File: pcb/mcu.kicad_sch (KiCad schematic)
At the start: 24 parts

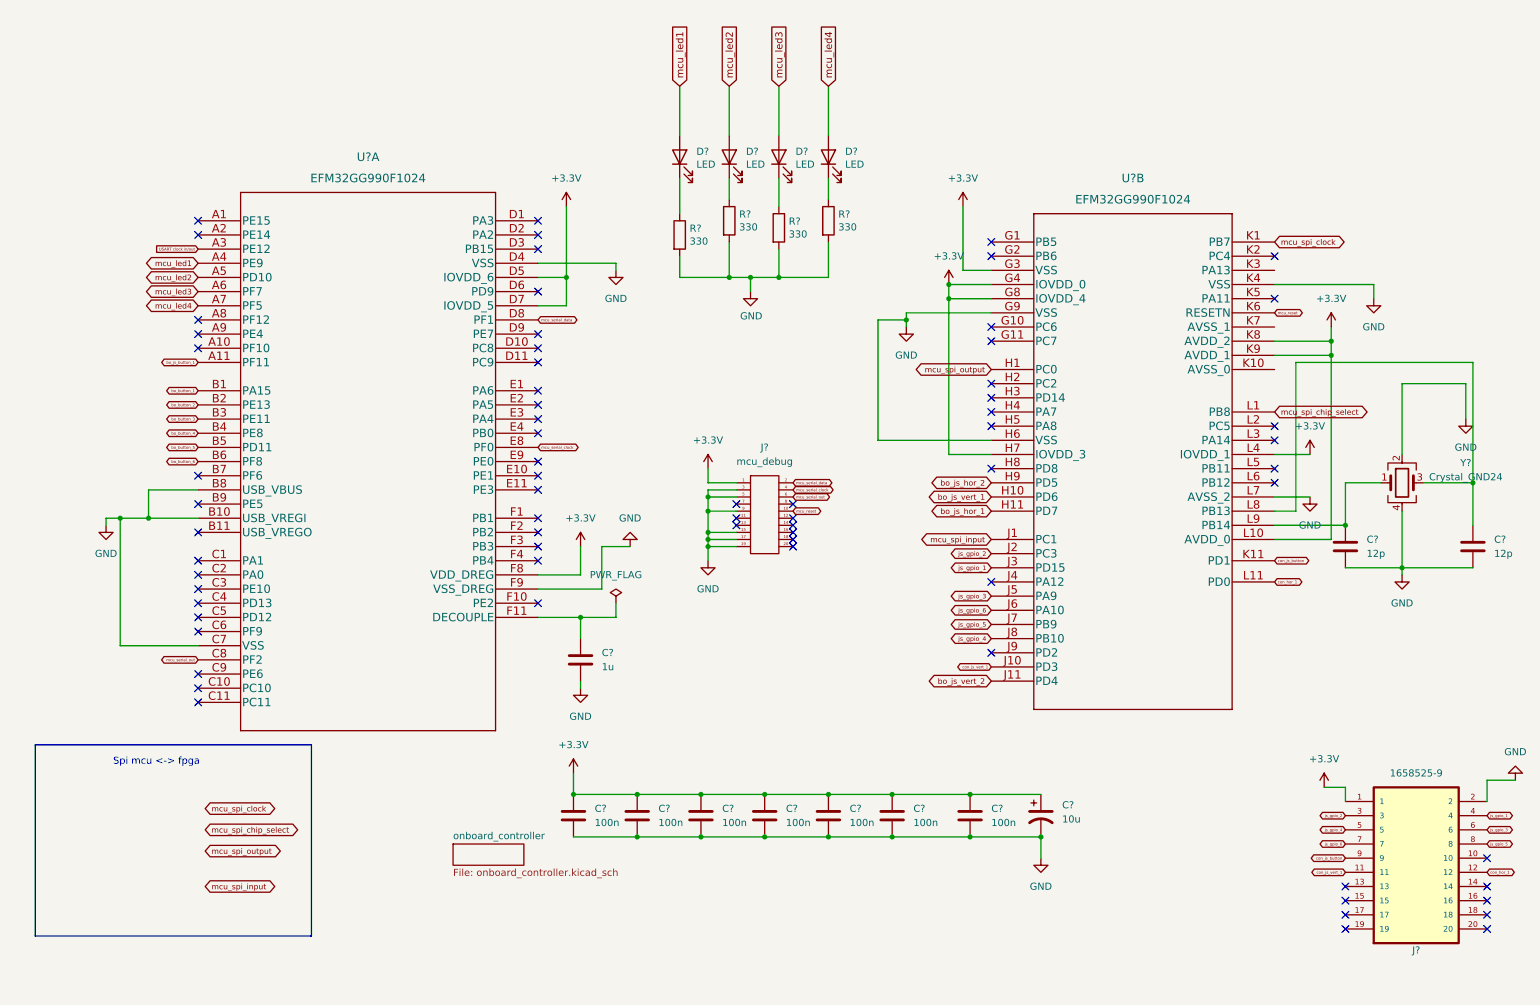
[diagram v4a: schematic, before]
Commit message: add capasitor values
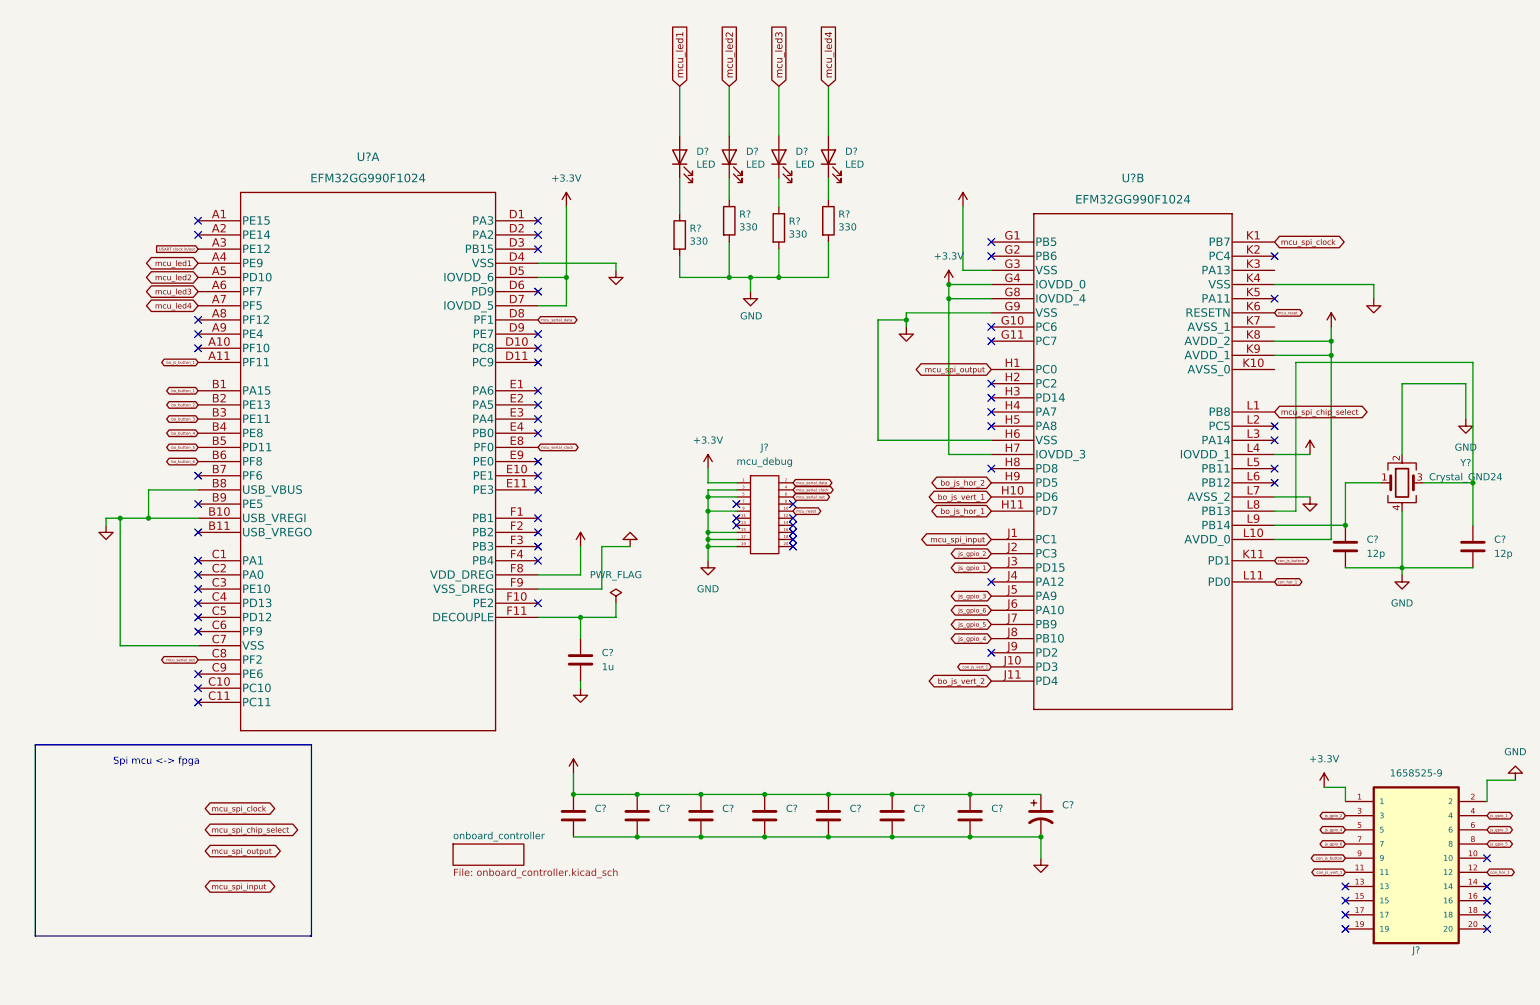
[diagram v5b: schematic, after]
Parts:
- C? (x7): value 100n -> (none)
- C?: value 10u -> (none)
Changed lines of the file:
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@@
       (effects (font (size 1.27 1.27)) hide)
     )
-    (property "Value" "+3.3V" (id 1) (at 111.76 142.24 0))
+    (property "Value" "" (id 1) (at 111.76 142.24 0))
     (property "Footprint" "" (id 2) (at 111.76 147.32 0)
       (effects (font (size 1.27 1.27)) hide)
@@
       (effects (font (size 1.27 1.27)) (justify left))
     )
-    (property "Value" "100n" (id 1) (at 172.72 156.2099 0)
+    (property "Value" "" (id 1) (at 172.72 156.2099 0)
       (effects (font (size 1.27 1.27)) (justify left))
     )
@@
       (effects (font (size 1.27 1.27)) hide)
     )
-    (property "Value" "GND" (id 1) (at 171.45 72.39 0))
+    (property "Value" "" (id 1) (at 171.45 72.39 0))
     (property "Footprint" "" (id 2) (at 171.45 67.31 0)
       (effects (font (size 1.27 1.27)) hide)
@@
       (effects (font (size 1.27 1.27)) hide)
     )
-    (property "Value" "+3.3V" (id 1) (at 243.84 85.09 0))
+    (property "Value" "" (id 1) (at 243.84 85.09 0))
     (property "Footprint" "" (id 2) (at 243.84 90.17 0)
       (effects (font (size 1.27 1.27)) hide)
@@
       (effects (font (size 1.27 1.27)) hide)
     )
-    (property "Value" "GND" (id 1) (at 27.94 107.95 0))
+    (property "Value" "" (id 1) (at 27.94 107.95 0))
     (property "Footprint" "" (id 2) (at 27.94 102.87 0)
       (effects (font (size 1.27 1.27)) hide)
@@
       (effects (font (size 1.27 1.27)) hide)
     )
-    (property "Value" "GND" (id 1) (at 243.84 102.87 0))
+    (property "Value" "" (id 1) (at 243.84 102.87 0))
     (property "Footprint" "" (id 2) (at 243.84 97.79 0)
       (effects (font (size 1.27 1.27)) hide)
@@
       (effects (font (size 1.27 1.27)) (justify left))
     )
-    (property "Value" "100n" (id 1) (at 161.29 156.2099 0)
+    (property "Value" "" (id 1) (at 161.29 156.2099 0)
       (effects (font (size 1.27 1.27)) (justify left))
     )
@@
       (effects (font (size 1.27 1.27)) hide)
     )
-    (property "Value" "GND" (id 1) (at 195.58 167.64 0))
+    (property "Value" "" (id 1) (at 195.58 167.64 0))
     (property "Footprint" "" (id 2) (at 195.58 162.56 0)
       (effects (font (size 1.27 1.27)) hide)
@@
       (effects (font (size 1.27 1.27)) hide)
     )
-    (property "Value" "GND" (id 1) (at 121.92 101.6 0))
+    (property "Value" "" (id 1) (at 121.92 101.6 0))
     (property "Footprint" "" (id 2) (at 121.92 106.68 0)
       (effects (font (size 1.27 1.27)) hide)
@@
       (effects (font (size 1.27 1.27)) hide)
     )
-    (property "Value" "GND" (id 1) (at 113.03 137.16 0))
+    (property "Value" "" (id 1) (at 113.03 137.16 0))
     (property "Footprint" "" (id 2) (at 113.03 132.08 0)
       (effects (font (size 1.27 1.27)) hide)
@@
       (effects (font (size 1.27 1.27)) hide)
     )
-    (property "Value" "+3.3V" (id 1) (at 247.65 62.23 0))
+    (property "Value" "" (id 1) (at 247.65 62.23 0))
     (property "Footprint" "" (id 2) (at 247.65 67.31 0)
       (effects (font (size 1.27 1.27)) hide)
@@
       (effects (font (size 1.27 1.27)) hide)
     )
-    (property "Value" "GND" (id 1) (at 255.27 67.31 0))
+    (property "Value" "" (id 1) (at 255.27 67.31 0))
     (property "Footprint" "" (id 2) (at 255.27 62.23 0)
       (effects (font (size 1.27 1.27)) hide)
@@
       (effects (font (size 1.27 1.27)) hide)
     )
-    (property "Value" "+3.3V" (id 1) (at 181.61 40.64 0))
+    (property "Value" "" (id 1) (at 181.61 40.64 0))
     (property "Footprint" "" (id 2) (at 181.61 45.72 0)
       (effects (font (size 1.27 1.27)) hide)
@@
       (effects (font (size 1.27 1.27)) hide)
     )
-    (property "Value" "GND" (id 1) (at 119.38 62.23 0))
+    (property "Value" "" (id 1) (at 119.38 62.23 0))
     (property "Footprint" "" (id 2) (at 119.38 57.15 0)
       (effects (font (size 1.27 1.27)) hide)
@@
       (effects (font (size 1.27 1.27)) hide)
     )
-    (property "Value" "+3.3V" (id 1) (at 113.03 101.6 0))
+    (property "Value" "" (id 1) (at 113.03 101.6 0))
     (property "Footprint" "" (id 2) (at 113.03 106.68 0)
       (effects (font (size 1.27 1.27)) hide)
@@
       (effects (font (size 1.27 1.27)) (justify left))
     )
-    (property "Value" "100n" (id 1) (at 138.43 156.2099 0)
+    (property "Value" "" (id 1) (at 138.43 156.2099 0)
       (effects (font (size 1.27 1.27)) (justify left))
     )
@@
       (effects (font (size 1.27 1.27)) (justify left))
     )
-    (property "Value" "100n" (id 1) (at 149.86 156.2099 0)
+    (property "Value" "" (id 1) (at 149.86 156.2099 0)
       (effects (font (size 1.27 1.27)) (justify left))
     )
@@
       (effects (font (size 1.27 1.27)) (justify left))
     )
-    (property "Value" "10u" (id 1) (at 199.39 155.5749 0)
+    (property "Value" "" (id 1) (at 199.39 155.5749 0)
       (effects (font (size 1.27 1.27)) (justify left))
     )
@@
       (effects (font (size 1.27 1.27)) (justify left))
     )
-    (property "Value" "100n" (id 1) (at 186.69 156.2099 0)
+    (property "Value" "" (id 1) (at 186.69 156.2099 0)
       (effects (font (size 1.27 1.27)) (justify left))
     )
@@
       (effects (font (size 1.27 1.27)) (justify left))
     )
-    (property "Value" "100n" (id 1) (at 127 156.2099 0)
+    (property "Value" "" (id 1) (at 127 156.2099 0)
       (effects (font (size 1.27 1.27)) (justify left))
     )
@@
       (effects (font (size 1.27 1.27)) (justify left))
     )
-    (property "Value" "100n" (id 1) (at 115.57 156.2099 0)
-      (effects (font (size 1.27 1.27)) (justify left))
-    )
+    (property "Value" "" (id 1) (at 115.57 156.2099 0)
+      (effects (font (size 1.27 1.27)) (justify left))
+    )

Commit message: add capasitro values again
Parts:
- C? (x8): value (none) -> ~
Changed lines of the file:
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@@
       (effects (font (size 1.27 1.27)) hide)
     )
-    (property "Value" "" (id 1) (at 111.76 142.24 0))
+    (property "Value" "~" (id 1) (at 111.76 142.24 0))
     (property "Footprint" "" (id 2) (at 111.76 147.32 0)
       (effects (font (size 1.27 1.27)) hide)
@@
       (effects (font (size 1.27 1.27)) (justify left))
     )
-    (property "Value" "" (id 1) (at 172.72 156.2099 0)
+    (property "Value" "~" (id 1) (at 172.72 156.2099 0)
       (effects (font (size 1.27 1.27)) (justify left))
     )
@@
       (effects (font (size 1.27 1.27)) hide)
     )
-    (property "Value" "" (id 1) (at 171.45 72.39 0))
+    (property "Value" "~" (id 1) (at 171.45 72.39 0))
     (property "Footprint" "" (id 2) (at 171.45 67.31 0)
       (effects (font (size 1.27 1.27)) hide)
@@
       (effects (font (size 1.27 1.27)) hide)
     )
-    (property "Value" "" (id 1) (at 243.84 85.09 0))
+    (property "Value" "~" (id 1) (at 243.84 85.09 0))
     (property "Footprint" "" (id 2) (at 243.84 90.17 0)
       (effects (font (size 1.27 1.27)) hide)
@@
       (effects (font (size 1.27 1.27)) hide)
     )
-    (property "Value" "" (id 1) (at 27.94 107.95 0))
+    (property "Value" "~" (id 1) (at 27.94 107.95 0))
     (property "Footprint" "" (id 2) (at 27.94 102.87 0)
       (effects (font (size 1.27 1.27)) hide)
@@
       (effects (font (size 1.27 1.27)) hide)
     )
-    (property "Value" "" (id 1) (at 243.84 102.87 0))
+    (property "Value" "~" (id 1) (at 243.84 102.87 0))
     (property "Footprint" "" (id 2) (at 243.84 97.79 0)
       (effects (font (size 1.27 1.27)) hide)
@@
       (effects (font (size 1.27 1.27)) (justify left))
     )
-    (property "Value" "" (id 1) (at 161.29 156.2099 0)
+    (property "Value" "~" (id 1) (at 161.29 156.2099 0)
       (effects (font (size 1.27 1.27)) (justify left))
     )
@@
       (effects (font (size 1.27 1.27)) hide)
     )
-    (property "Value" "" (id 1) (at 195.58 167.64 0))
+    (property "Value" "~" (id 1) (at 195.58 167.64 0))
     (property "Footprint" "" (id 2) (at 195.58 162.56 0)
       (effects (font (size 1.27 1.27)) hide)
@@
       (effects (font (size 1.27 1.27)) hide)
     )
-    (property "Value" "" (id 1) (at 121.92 101.6 0))
+    (property "Value" "~" (id 1) (at 121.92 101.6 0))
     (property "Footprint" "" (id 2) (at 121.92 106.68 0)
       (effects (font (size 1.27 1.27)) hide)
@@
       (effects (font (size 1.27 1.27)) hide)
     )
-    (property "Value" "" (id 1) (at 113.03 137.16 0))
+    (property "Value" "~" (id 1) (at 113.03 137.16 0))
     (property "Footprint" "" (id 2) (at 113.03 132.08 0)
       (effects (font (size 1.27 1.27)) hide)
@@
       (effects (font (size 1.27 1.27)) hide)
     )
-    (property "Value" "" (id 1) (at 247.65 62.23 0))
+    (property "Value" "~" (id 1) (at 247.65 62.23 0))
     (property "Footprint" "" (id 2) (at 247.65 67.31 0)
       (effects (font (size 1.27 1.27)) hide)
@@
       (effects (font (size 1.27 1.27)) hide)
     )
-    (property "Value" "" (id 1) (at 255.27 67.31 0))
+    (property "Value" "~" (id 1) (at 255.27 67.31 0))
     (property "Footprint" "" (id 2) (at 255.27 62.23 0)
       (effects (font (size 1.27 1.27)) hide)
@@
       (effects (font (size 1.27 1.27)) hide)
     )
-    (property "Value" "" (id 1) (at 181.61 40.64 0))
+    (property "Value" "~" (id 1) (at 181.61 40.64 0))
     (property "Footprint" "" (id 2) (at 181.61 45.72 0)
       (effects (font (size 1.27 1.27)) hide)
@@
       (effects (font (size 1.27 1.27)) hide)
     )
-    (property "Value" "" (id 1) (at 119.38 62.23 0))
+    (property "Value" "~" (id 1) (at 119.38 62.23 0))
     (property "Footprint" "" (id 2) (at 119.38 57.15 0)
       (effects (font (size 1.27 1.27)) hide)
@@
       (effects (font (size 1.27 1.27)) hide)
     )
-    (property "Value" "" (id 1) (at 113.03 101.6 0))
+    (property "Value" "~" (id 1) (at 113.03 101.6 0))
     (property "Footprint" "" (id 2) (at 113.03 106.68 0)
       (effects (font (size 1.27 1.27)) hide)
@@
       (effects (font (size 1.27 1.27)) (justify left))
     )
-    (property "Value" "" (id 1) (at 138.43 156.2099 0)
+    (property "Value" "~" (id 1) (at 138.43 156.2099 0)
       (effects (font (size 1.27 1.27)) (justify left))
     )
@@
       (effects (font (size 1.27 1.27)) (justify left))
     )
-    (property "Value" "" (id 1) (at 149.86 156.2099 0)
+    (property "Value" "~" (id 1) (at 149.86 156.2099 0)
       (effects (font (size 1.27 1.27)) (justify left))
     )
@@
       (effects (font (size 1.27 1.27)) (justify left))
     )
-    (property "Value" "" (id 1) (at 199.39 155.5749 0)
+    (property "Value" "~" (id 1) (at 199.39 155.5749 0)
       (effects (font (size 1.27 1.27)) (justify left))
     )
@@
       (effects (font (size 1.27 1.27)) (justify left))
     )
-    (property "Value" "" (id 1) (at 186.69 156.2099 0)
+    (property "Value" "~" (id 1) (at 186.69 156.2099 0)
       (effects (font (size 1.27 1.27)) (justify left))
     )
@@
       (effects (font (size 1.27 1.27)) (justify left))
     )
-    (property "Value" "" (id 1) (at 127 156.2099 0)
+    (property "Value" "~" (id 1) (at 127 156.2099 0)
       (effects (font (size 1.27 1.27)) (justify left))
     )
@@
       (effects (font (size 1.27 1.27)) (justify left))
     )
-    (property "Value" "" (id 1) (at 115.57 156.2099 0)
-      (effects (font (size 1.27 1.27)) (justify left))
-    )
+    (property "Value" "~" (id 1) (at 115.57 156.2099 0)
+      (effects (font (size 1.27 1.27)) (justify left))
+    )

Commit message: add missing values again
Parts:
- removed C? (x7): ~, symbol Device:C
- added C? (x7): 100n, symbol Device:C
- C?: value ~ -> 10u
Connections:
- net +3.3V: now also C?.1, C?.1, C?.1, C?.1, C?.1, C?.1, C?.1
- net GND: now also C?.2, C?.2, C?.2, C?.2, C?.2, C?.2, C?.2

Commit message: maybe finished schematic
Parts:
- removed C? (x2): 12p, symbol Device:C
- removed D? (x4): LED, LED_SMD:LED_1206_3216Metric_Pad1.42x1.75mm_HandSolder, symbol Device:LED
- removed J?: mcu_debug, symbol datamaskin:mcu_debug
- removed R? (x4): 330, Resistor_SMD:R_2512_6332Metric_Pad1.40x3.35mm_HandSolder, symbol Device:R
- removed Y?: Crystal_GND24, symbol Device:Crystal_GND24
- added C? (x2): 12p, symbol Device:C
- added Y?: Crystal_GND24, symbol Device:Crystal_GND24
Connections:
- net GND: now also U?.K10 (AVSS_0), C?.2, C?.2, Y?.2, Y?.4
- net bo_button_2: now also U?.B3 (PE11); no longer U?.B2 (PE13)
- net bo_button_3: now also U?.B4 (PE8); no longer U?.B3 (PE11)
- net bo_button_4: now also U?.B5 (PD11); no longer U?.B4 (PE8)
- net bo_button_5: now also U?.B6 (PF8); no longer U?.B5 (PD11)
- net bo_button_6: now also U?.B7 (PF6); no longer U?.B6 (PF8)
- net at U?.L8 (PB13): now also C?.1, Y?.3
- net at U?.L9 (PB14): now also C?.1, Y?.1
- net MCU_SD_US0_MOSI: now reaches U?.C10 (PC10)
- net MCU_SD_US0_MISO: now reaches U?.C11 (PC11)
- net SD_CARD_DETECT: now reaches U?.C9 (PE6)
- net FPGA_MCU_EXTRA1: now reaches U?.D1 (PA3)
- net FPGA_MCU_EXTRA2: now reaches U?.D2 (PA2)
- net PROGRAM_B: now reaches U?.E1 (PA6)
- net DONE: now reaches U?.E2 (PA5)
- net USART clock in/out renamed MCU_SD_US0_CLK
- net mcu_serial_clock renamed mcu_debug_serial_clock
- net mcu_serial_data renamed mcu_debug_serial_data
- net mcu_serial_out renamed mcu_debug_serial_out
- net mcu_spi_chip_select renamed MCU_FPGA_US1_CS
- net mcu_spi_clock renamed MCU_FPGA_US1_CLK
- net mcu_spi_input renamed MCU_FPGA_US1_MISO
- net mcu_spi_output renamed MCU_FPGA_US1_MOSI
- new net MCU_SD_US0_CS: U?.B2 (PE13)
- no-connect marks 71 -> 55
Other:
- added sheet MCU_DEBUG (MCU_DEBUG.kicad_sch)
- added sheet MCU_DEBUG_LEDS (MCU_DEBUG_LEDS.kicad_sch)
- added sheet sd (sd.kicad_sch)
- note added: "Controler headers"
- note removed: "Spi mcu <-> fpga"
- moved on the sheet: C?, J?, U?A, U?B
